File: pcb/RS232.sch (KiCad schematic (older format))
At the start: 7 parts, among them IC3 ICL3221EIVZ, J16 DB9_Male_MountingHoles

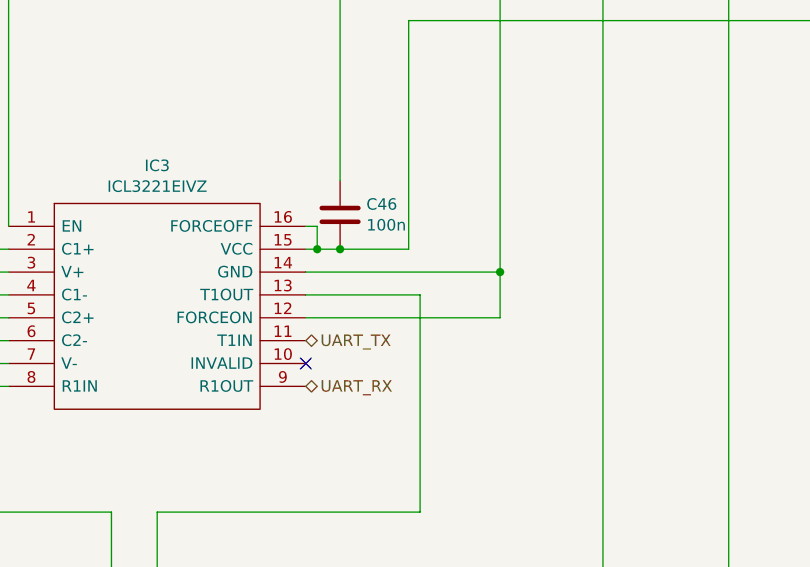
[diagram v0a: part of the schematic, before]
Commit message: Pull FORCEON to high on RS232 to avoid standby, fixed #18. Also implemented virtual symbol for permanent fiducials
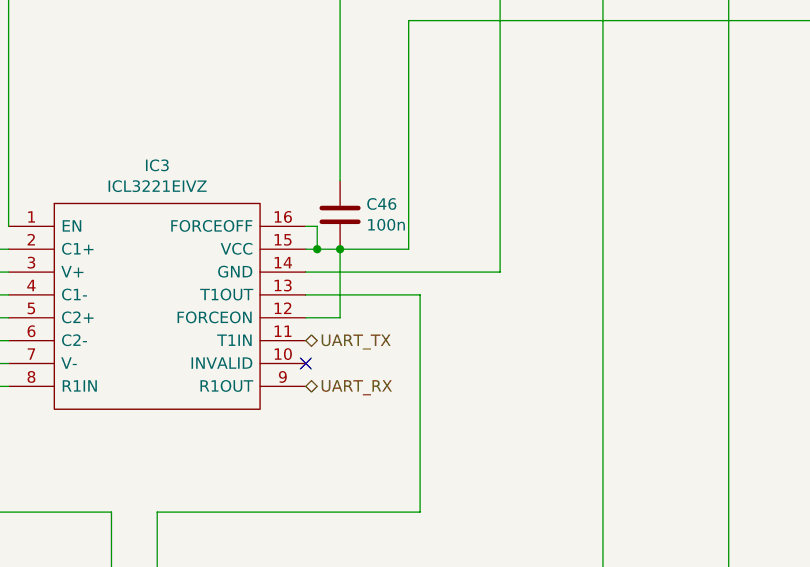
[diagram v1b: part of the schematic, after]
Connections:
- net +3V3: now also IC3.12 (FORCEON)
- net GND: no longer IC3.12 (FORCEON)
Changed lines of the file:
@@
 Wire Wire Line
 	7100 1750 6400 1750
-Wire Wire Line
-	6250 3200 7100 3200
-Wire Wire Line
-	7100 3200 7100 3000
-Connection ~ 7100 3000
 Text HLabel 6250 3300 2    50   BiDi ~ 0
 UART_TX
@@
 Wire Wire Line
 	8100 1750 7550 1750
+Wire Wire Line
+	6400 2900 6400 3200
+Wire Wire Line
+	6400 3200 6250 3200
 $EndSCHEMATC
